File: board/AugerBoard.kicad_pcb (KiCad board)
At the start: 2 copper layers, 96.5 x 99.1 mm, 81 parts, among them J1 RJ45_LED_Shielded, J2 Conn_01x04_MountingPin, Q1 BSS138, Q2 BSS138, Q3 BSS138, Q4 BSS138, Q5 BSS138, Q6 BSS138, Q7 BSS138, Q8 BSS138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

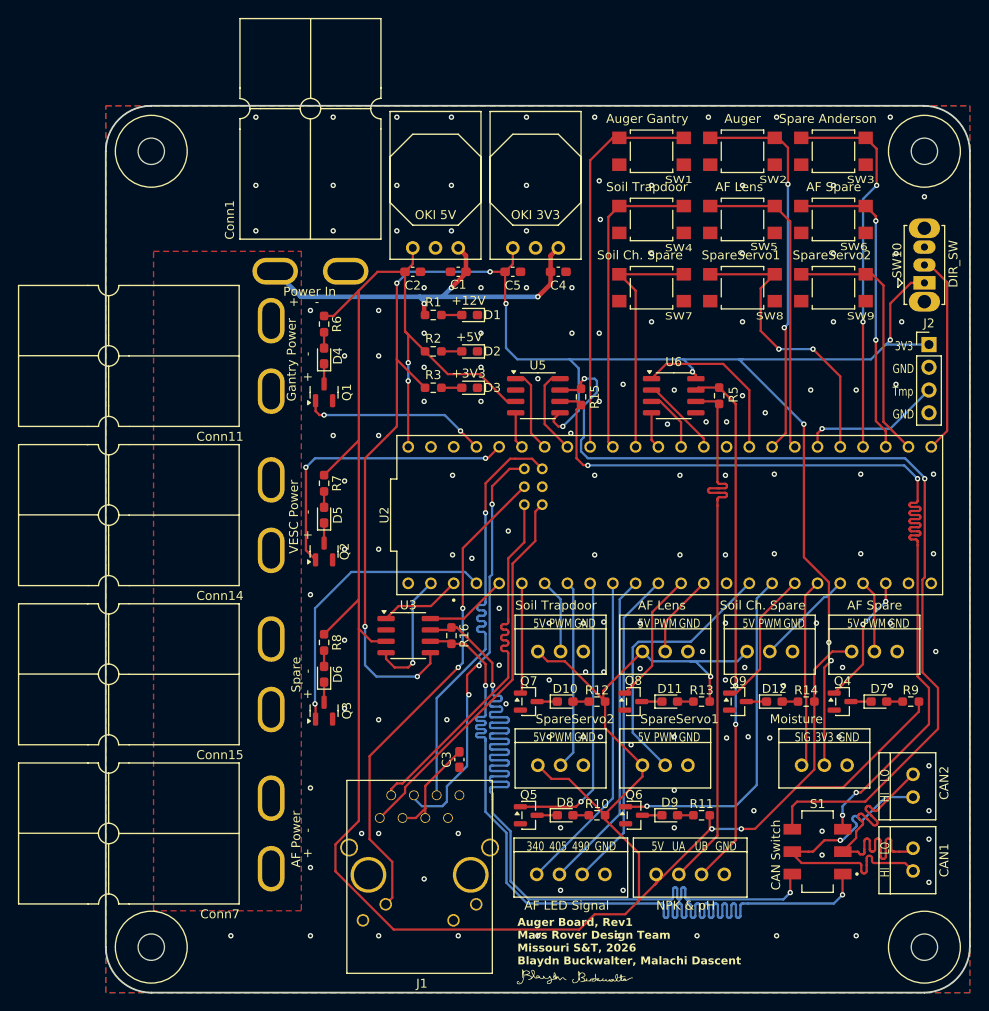
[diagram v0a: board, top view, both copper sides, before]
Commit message: Redid layout to shrink & add new power connectors
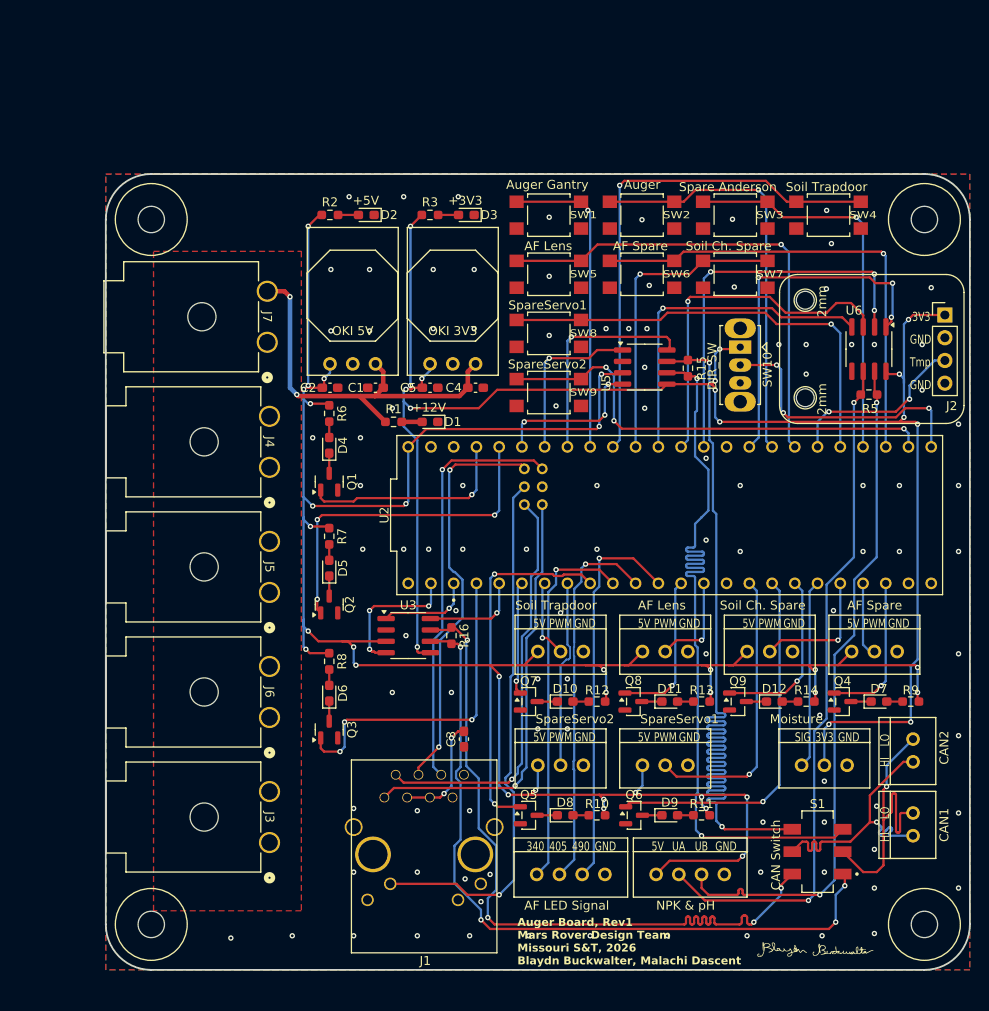
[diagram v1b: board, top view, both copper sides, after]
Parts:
- removed Conn1, Conn11, Conn14, Conn15, Conn7: AndersonPP, MRDT_Connectors:Square_Anderson_2_H_Side_By_Side_PV
- added 2mm: MountingHole_2mm, MountingHole:MountingHole_2mm, F.Cu at (141.6, 80.1)
- added 2mm: MountingHole_2mm, MountingHole:MountingHole_2mm, F.Cu at (141.6, 91.0)
- added J3: 2002411212, footprints:CONN_2002412000_02_MOL, F.Cu at (81.8, 140.7)
- added J4: 2002411212, footprints:CONN_2002412000_02_MOL, F.Cu at (81.8, 98.8)
- added J5: 2002411212, footprints:CONN_2002412000_02_MOL, F.Cu at (81.8, 112.8)
- added J6: 2002411212, footprints:CONN_2002412000_02_MOL, F.Cu at (81.8, 126.7)
- added J7: 2002411212, footprints:CONN_2002412000_02_MOL, F.Cu at (81.5, 84.8)
- moved SW9 33.9 mm to (113.0, 90.4)
- moved G*** 27.0 mm to (143.4, 152.9)
- moved SW5 22.5 mm to (113.0, 77.2)
- moved U6 22.4 mm to (148.7, 85.6), turned to -90 degrees
- moved SW6 22.2 mm to (123.4, 77.2)
- moved SW8 22.2 mm to (113.0, 83.8)
- moved SW10 21.8 mm to (134.4, 85.4), turned to -90 degrees
- moved SW4 19.8 mm to (144.2, 70.6)
- moved D3 19.3 mm to (103.8, 70.6)
- moved R3 19.3 mm to (99.7, 70.6)
- moved D2 19.1 mm to (92.6, 70.6)
- moved R2 19.1 mm to (88.5, 70.6)
- moved R5 16.7 mm to (148.7, 90.7), turned to 0 degrees
- moved C1 15.9 mm to (93.6, 89.9)
- moved C2 15.9 mm to (88.5, 89.9)
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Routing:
- net /Soil Sensors & NPK/RE: track 8.60 -> 44.2 mm, vias 0 -> 3
- net /Soil Sensors & NPK/DI: track 4.13 -> 37.7 mm, vias 0 -> 1
- net /Soil Sensors & NPK/DE: track 7.02 -> 39.6 mm, vias 0 -> 1
- net /Teensy/SpareSW2: track 28.9 -> 51.9 mm, vias 0 -> 3
- net Net-(U3-CANL): track 104.5 -> 81.6 mm, vias 2 -> 4
- net /Teensy/SoilDoorSW: track 34.8 -> 57.6 mm, vias 0 -> 1
- net Net-(U3-CANH): track 104.4 -> 81.7 mm, vias 2 -> 4
- net /Soil Sensors & NPK/RO: track 19.2 -> 39.8 mm, vias 0 -> 3
- net /Teensy/AFLensSW: track 35.0 -> 53.5 mm, vias 0 -> 1
- net /Teensy/AFSpareSW: track 35.0 -> 52.8 mm, vias 2 -> 1
- net Net-(U6-B): track 59.4 -> 76.9 mm
- net /Teensy/SpareSW1: track 33.0 -> 50.1 mm, vias 2 -> 1
- net Net-(U5-CANL): track 101.5 -> 85.3 mm, vias 4 -> 2
- net /Communications/STBY2: track 9.95 -> 24.9 mm, vias 0 -> 1
- net Net-(U6-A): track 62.0 -> 76.8 mm, vias 0 -> 2
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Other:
- board size 96.5 x 99.1 mm -> 96.5 x 88.9 mm
- board text removed: "+ -"
- board text removed: "AF Power"
- board text removed: "Gantry Power"
- board text removed: "Power In"
- board text removed: "Spare"
- board text removed: "VESC Power"

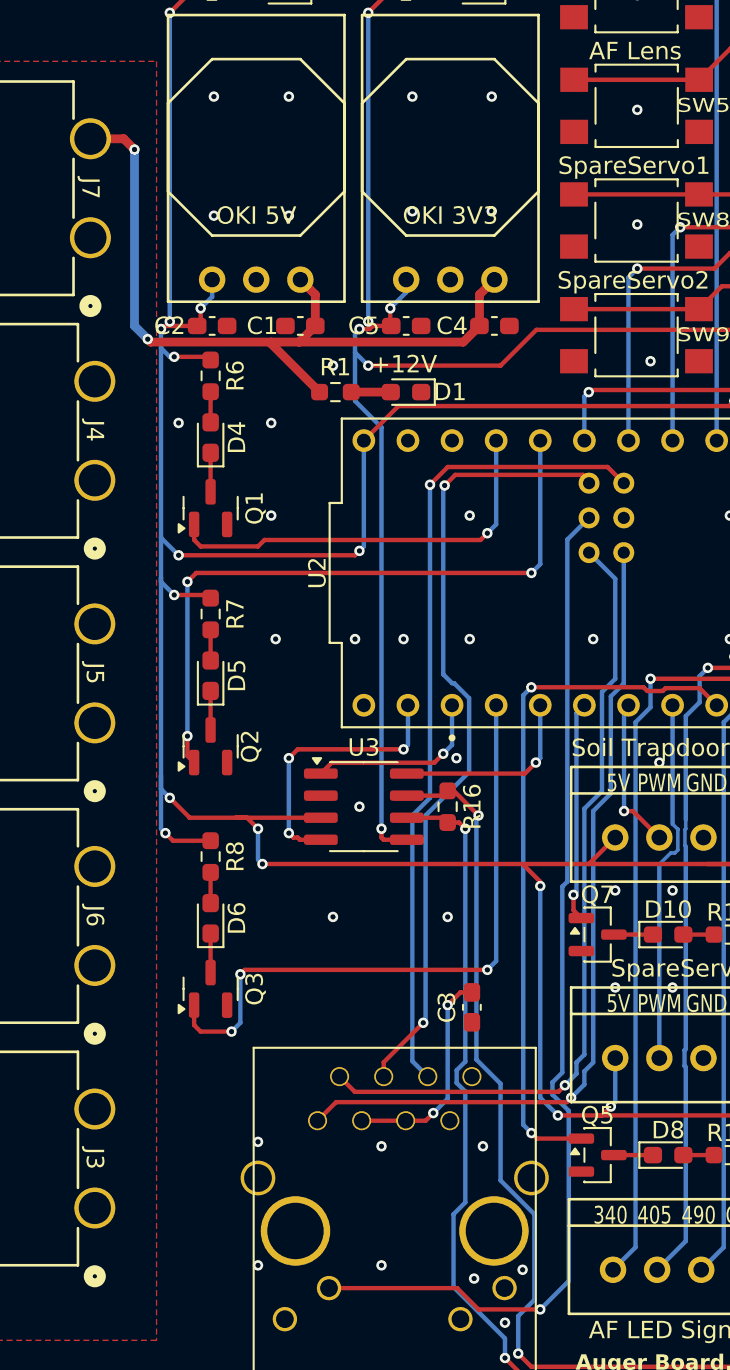
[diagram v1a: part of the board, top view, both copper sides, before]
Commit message: Added labels for power and fixed diff pair lengths
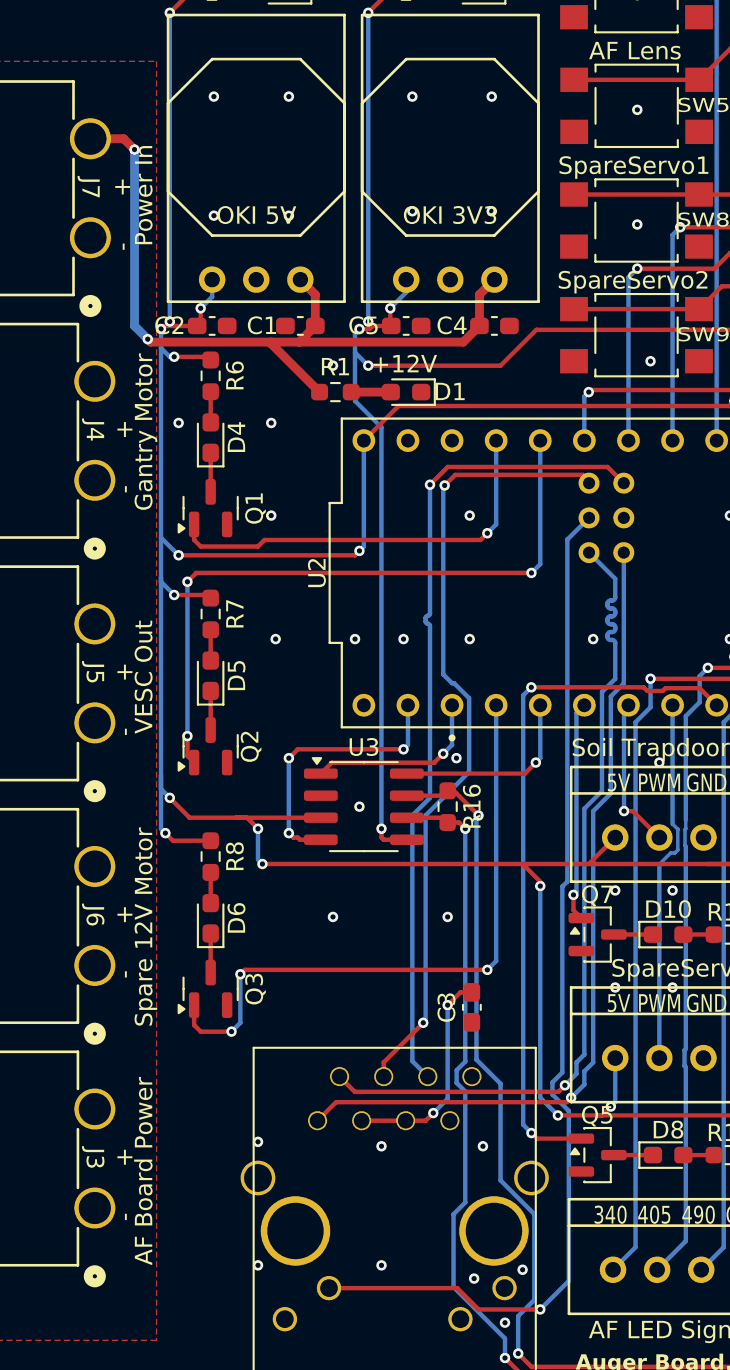
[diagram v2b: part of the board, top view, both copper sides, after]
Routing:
- net /Communications/T-: track 46.0 -> 47.7 mm
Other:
- board text added: "- +"
- board text added: "AF Board Power"
- board text added: "Gantry Motor"
- board text added: "Power In"
- board text added: "Spare 12V Motor"
- board text added: "VESC Out"

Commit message: fine tuning
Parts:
- J3, J4, J5, J6, J7: footprint footprints:CONN_2002412000_02_MOL -> footprints:CONN_SD-76825-0100_02_MOL
- moved J3 6.73 mm to (75.7, 137.8)
- moved J4 6.73 mm to (75.7, 95.9)
- moved J5 6.73 mm to (75.7, 109.8)
- moved J6 6.73 mm to (75.7, 123.8)
- moved J7 6.51 mm to (75.7, 81.9)
- moved G*** 0.68 mm to (143.7, 153.5)
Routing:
- net Net-(U5-CANH): track 105.2 -> 84.9 mm
- net +12V: track 45.0 -> 41.2 mm, vias 2 -> 1

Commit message: made changes from layout review
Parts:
- added G***: LOGO, MRDT_Silkscreens:0_MRDT_Logo_10mm, F.Cu at (79.0, 71.9)
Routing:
- net +12V: track 41.2 -> 30.7 mm, vias 1 -> 0
- net +5V: track 289.2 -> 290.6 mm, vias 32 -> 31
- net +3.3V: vias 16 -> 15
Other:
- board text added: "Auger VESC"
- board text added: "CAN"
- board text added: "Spare 12V"
- board text removed: "Spare Anderson"
- board text removed: "VESC Out"

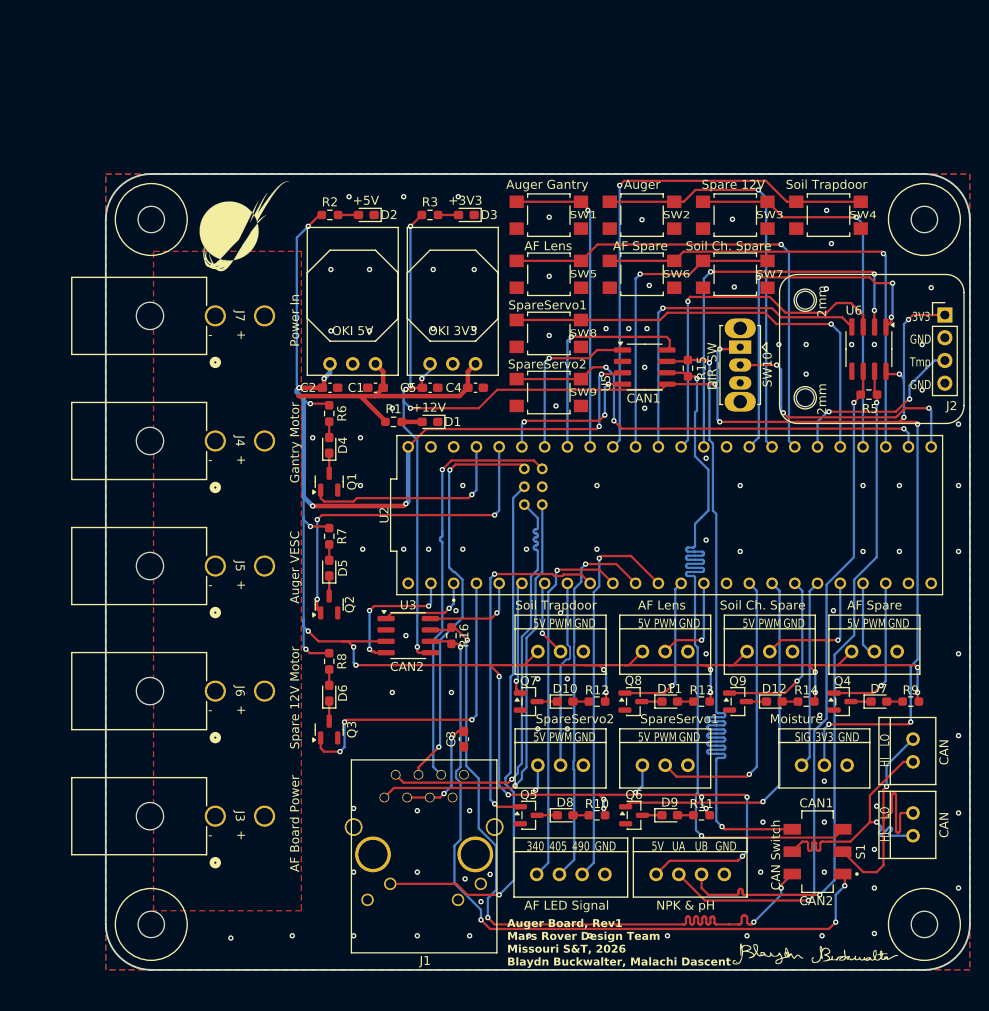
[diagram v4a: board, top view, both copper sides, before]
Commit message: added pin for AF, added gimbal names, refined look
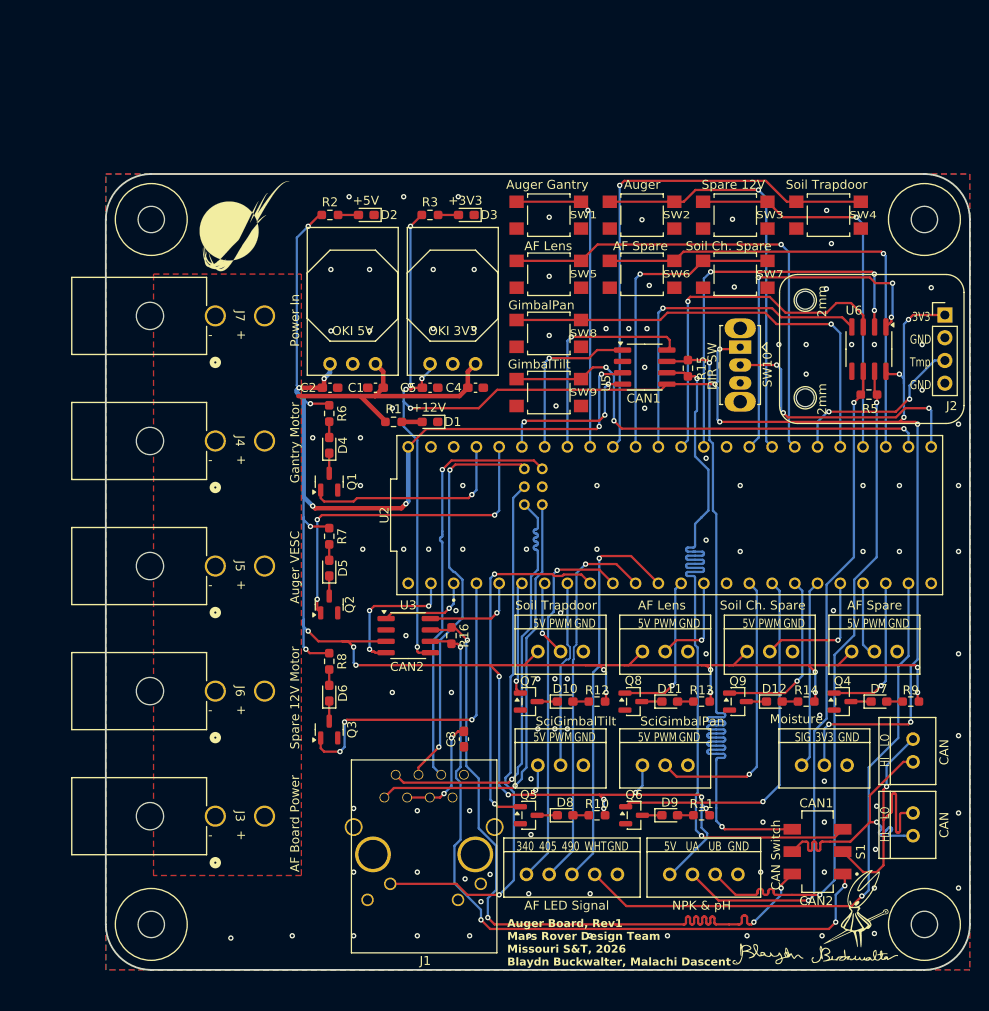
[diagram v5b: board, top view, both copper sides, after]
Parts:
- removed Conn8: Molex_uF_D_04, MRDT_Connectors:MOLEX_SL_04_Vertical
- added Conn1: Molex_SL_05, MRDT_Connectors:MOLEX_SL_05_Vertical, F.Cu at (110.5, 144.3)
- added G***: LOGO, LOGO, F.Cu at (147.3, 148.1)
- added G***: LOGO, LOGO, B.Cu at (111.8, 109.7)
- moved Conn16 1.52 mm to (126.5, 144.3)
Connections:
- net /Power/SpareServoLED1 renamed /Power/GimbalPanLED
- net /Power/SpareServoLED2 renamed /Power/GimbalTiltLED
- net /Servos/SparePWM1 renamed /Servos/SciGimbalPan
- net /Servos/SparePWM2 renamed /Servos/SciGimbalTilt
- net /Teensy/SpareSW1 renamed /Teensy/GimbalPanSW
- net /Teensy/SpareSW2 renamed /Teensy/GimbalTiltSW
- U2 pad 31: unconnected-(U2-CTX3-Pad31) -> /AF interface/AFWhiteLED
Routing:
- net /AF interface/AFWhiteLED: track 0.00 -> 68.9 mm, vias 0 -> 1
- net +5V: track 290.6 -> 278.0 mm, vias 31 -> 29
- net Net-(U6-B): track 76.9 -> 75.2 mm
- net Net-(U6-A): track 76.8 -> 75.3 mm
- net GND: vias 101 -> 107
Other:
- board text added: "GimbalPan"
- board text added: "GimbalTilt"
- board text added: "SciGimbalPan"
- board text added: "SciGimbalTilt"
- board text added: "WHT"
- board text removed: "SpareServo1"
- board text removed: "SpareServo2"

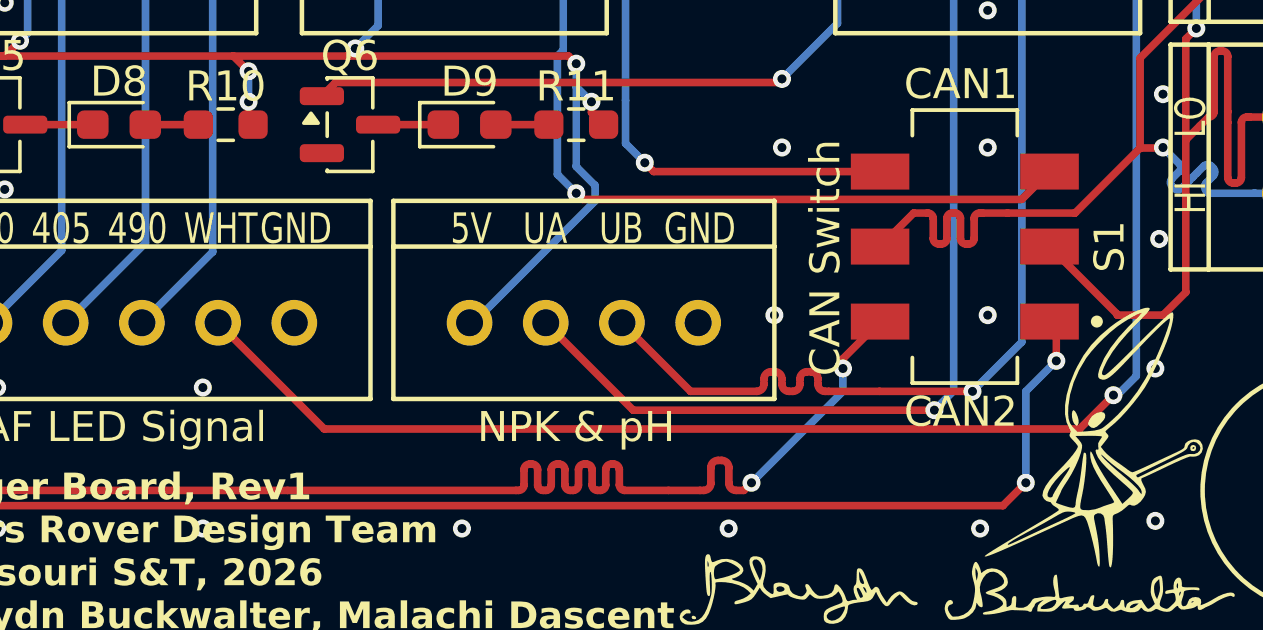
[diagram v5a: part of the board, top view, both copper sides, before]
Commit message: Swapped Pins for AF
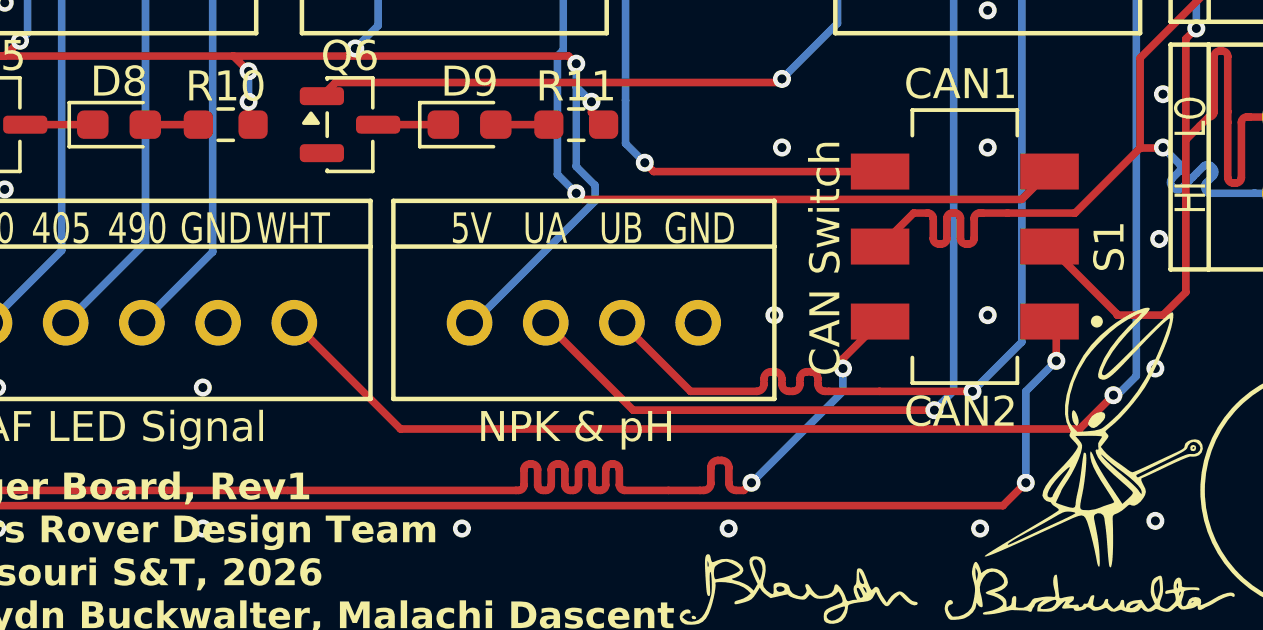
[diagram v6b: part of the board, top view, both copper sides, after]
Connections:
- Conn1 pad 4: /AF interface/AFWhiteLED -> GND
- Conn1 pad 5: GND -> /AF interface/AFWhiteLED
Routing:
- net /AF interface/AFWhiteLED: track 68.9 -> 66.4 mm
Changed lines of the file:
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@@
 			(layers "*.Cu" "*.Mask")
 			(remove_unused_layers no)
-			(net 54 "/AF interface/AFWhiteLED")
+			(net 1 "GND")
 			(pintype "input")
 		)
@@
 			(layers "*.Cu" "*.Mask")
 			(remove_unused_layers no)
-			(net 1 "GND")
+			(net 54 "/AF interface/AFWhiteLED")
 			(pintype "input")
 		)
@@
 	)
 	(gr_text "GND"
-		(at 119.507 141.732 0)
+		(at 116.84 141.732 0)
 		(layer "F.SilkS")
 		(effects
@@
 	)
 	(gr_text "WHT"
-		(at 116.967 141.732 0)
+		(at 119.38 141.732 0)
 		(layer "F.SilkS")
 		(effects
@@
 	)
 	(segment
-		(start 146.827 147.813)
-		(end 121.651 147.813)
+		(start 124.191 147.813)
+		(end 120.65 144.272)
 		(width 0.254)
 		(layer "F.Cu")
@@
 	)
 	(segment
-		(start 121.651 147.813)
-		(end 118.11 144.272)
+		(start 146.827 147.813)
+		(end 124.191 147.813)
 		(width 0.254)
 		(layer "F.Cu")
